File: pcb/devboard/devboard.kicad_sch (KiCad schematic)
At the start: 17 parts, among them J1 USB4110GFA, J3 Conn_01x16_Pin, J4 Conn_01x16_Pin, SW1 PTS526_SM15_SMTR2_LFS, SW2 PTS526_SM15_SMTR2_LFS, U1 ESP32-S3-MINI-1U, U2 IP4234CZ6, U3 ADP2108AUJ-3.3

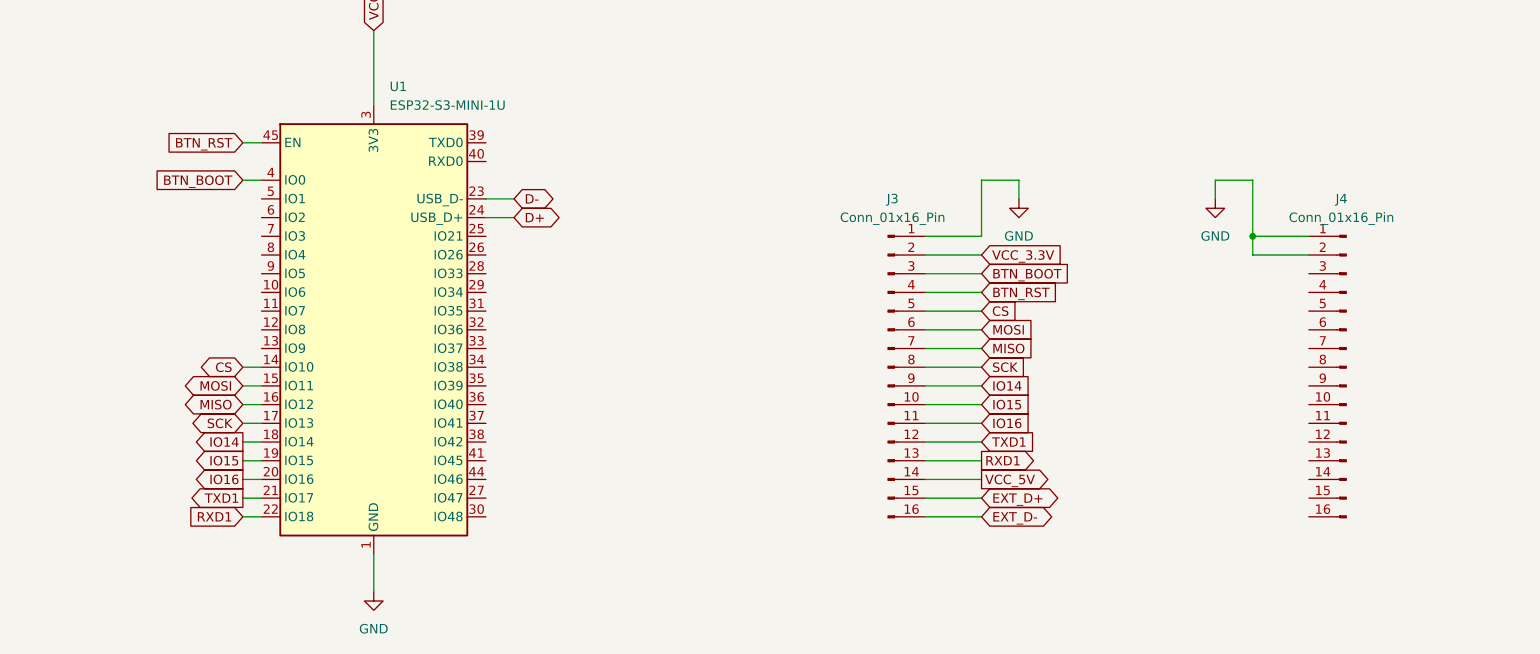
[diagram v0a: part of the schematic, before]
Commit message: connecting all remaining IOs
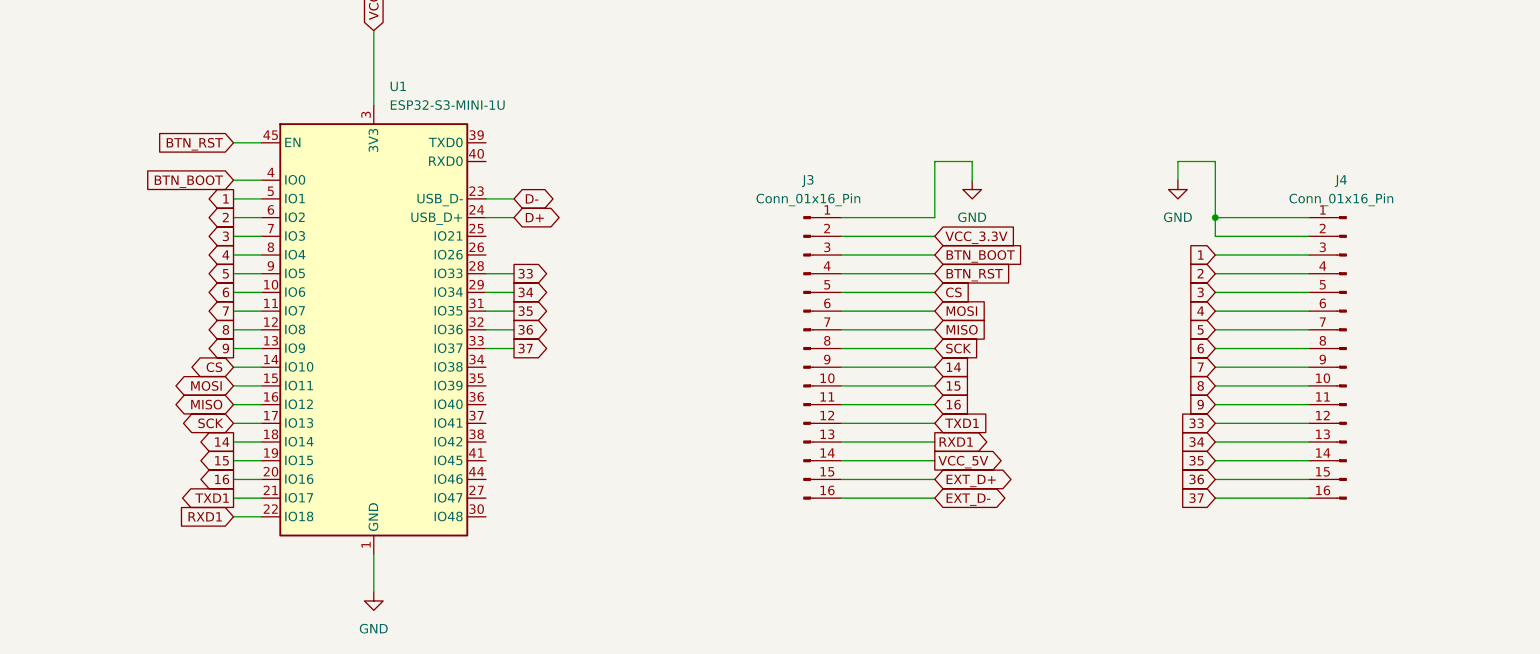
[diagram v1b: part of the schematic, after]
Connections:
- net 6: now reaches U1.10 (IO6)
- net 6: now also J4.8 (Pin_8)
- net 7: now reaches U1.11 (IO7)
- net 7: now also J4.9 (Pin_9)
- net 8: now reaches U1.12 (IO8)
- net 8: now also J4.10 (Pin_10)
- net 9: now reaches U1.13 (IO9)
- net 9: now also J4.11 (Pin_11)
- net 33: now reaches U1.28 (IO33)
- net 33: now also J4.12 (Pin_12)
- net 34: now reaches U1.29 (IO34)
- net 34: now also J4.13 (Pin_13)
- net 35: now reaches U1.31 (IO35)
- net 35: now also J4.14 (Pin_14)
- net 36: now reaches U1.32 (IO36)
- net 36: now also J4.15 (Pin_15)
- net 37: now reaches U1.33 (IO37)
- net 37: now also J4.16 (Pin_16)
- net 1: now reaches U1.5 (IO1)
- net 1: now also J4.3 (Pin_3)
- net 2: now reaches U1.6 (IO2)
- net 2: now also J4.4 (Pin_4)
- net 3: now reaches U1.7 (IO3)
- net 3: now also J4.5 (Pin_5)
- net 4: now reaches U1.8 (IO4)
- net 4: now also J4.6 (Pin_6)
- net 5: now reaches U1.9 (IO5)
- net 5: now also J4.7 (Pin_7)
- net IO14 renamed 14
- net IO15 renamed 15
- net IO16 renamed 16
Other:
- moved on the sheet: J3, J4

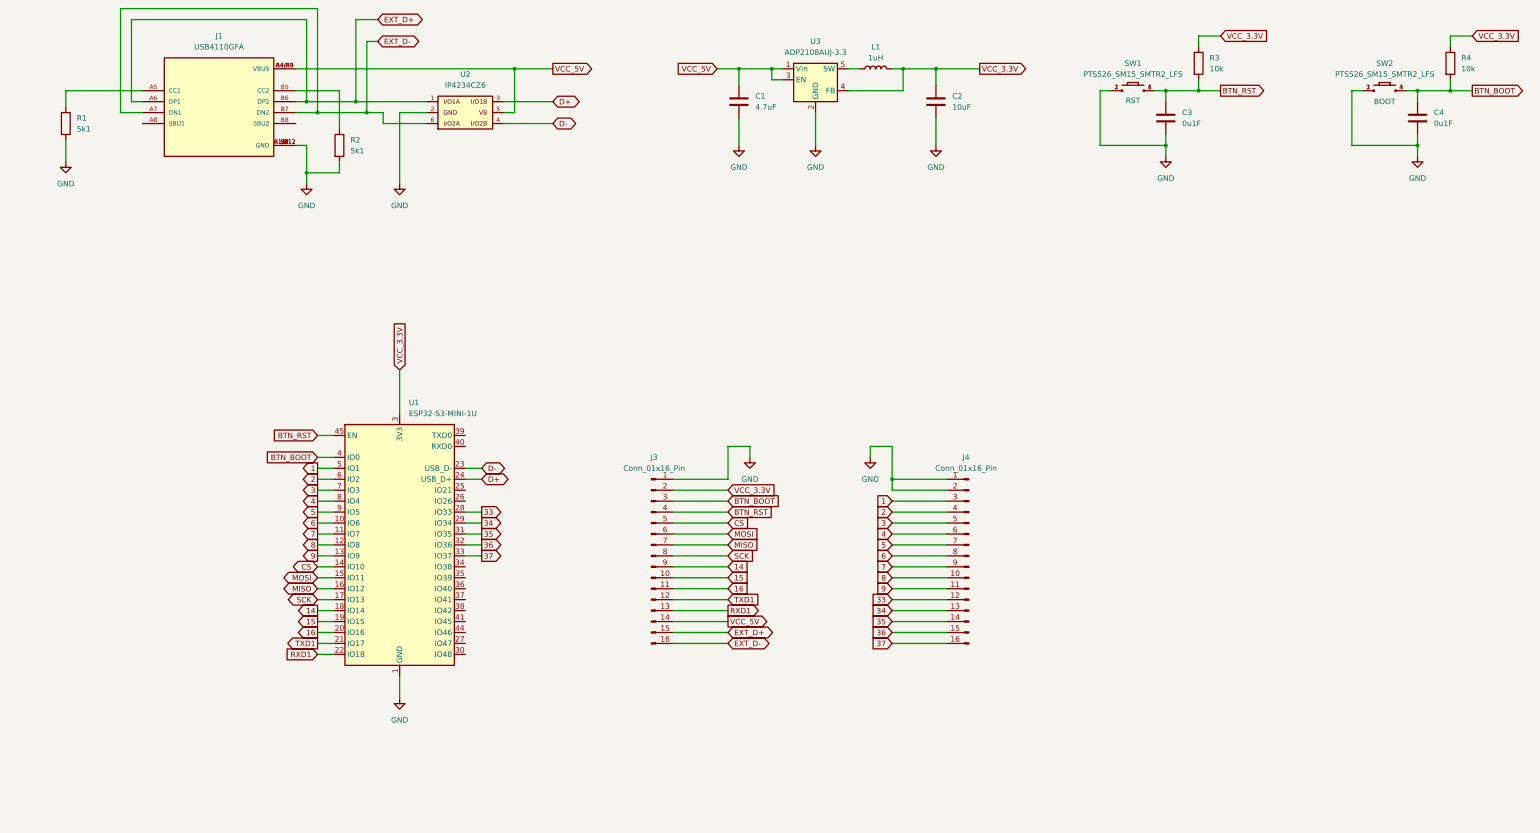
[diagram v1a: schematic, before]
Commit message: adding mouser part number to all parts
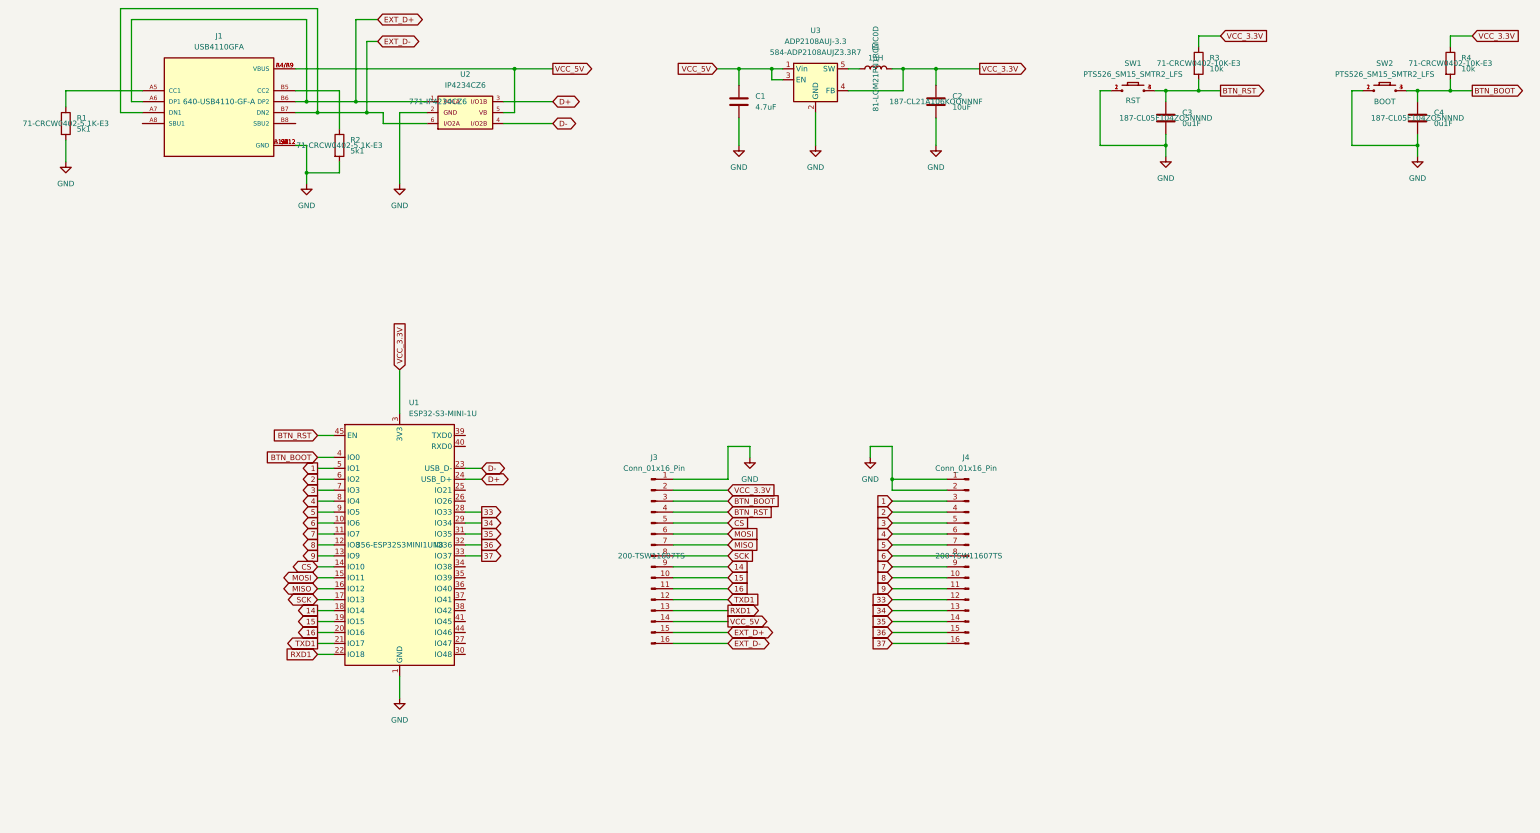
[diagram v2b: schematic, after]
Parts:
- C1: MOUSER_PART_NUMBER (none) -> 187-CL10A475KO8NNNC
- C2: MOUSER_PART_NUMBER (none) -> 187-CL21A106KOQNNNF
- C3, C4: MOUSER_PART_NUMBER (none) -> 187-CL05F104ZO5NNND
- J1: MOUSER_PART_NUMBER (none) -> 640-USB4110-GF-A
- J3, J4: MOUSER_PART_NUMBER (none) -> 200-TSW11607TS
- L1: MOUSER_PART_NUMBER (none) -> 81-LQM21PN1R0MC0D
- R1, R2: footprint (none) -> Resistor_SMD:R_0402_1005Metric; MOUSER_PART_NUMBER (none) -> 71-CRCW0402-5.1K-E3
- R3, R4: footprint (none) -> Resistor_SMD:R_0402_1005Metric; MOUSER_PART_NUMBER (none) -> 71-CRCW0402-10K-E3
- U1: MOUSER_PART_NUMBER (none) -> 356-ESP32S3MINI1UN8
- U2: MOUSER_PART_NUMBER (none) -> 771-IP4234CZ6
- U3: MOUSER_PART_NUMBER (none) -> 584-ADP2108AUJZ3.3R7
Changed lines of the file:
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@@
+			)
+		)
+		(property "MOUSER_PART_NUMBER" "771-IP4234CZ6"
+			(at 135.89 64.77 0)
+			(effects
+				(font
+					(size 1.27 1.27)
+				)
 			)
 		)
@@
 			)
 		)
-		(property "Footprint" ""
+		(property "Footprint" "Resistor_SMD:R_0402_1005Metric"
 			(at 47.752 69.85 90)
 			(effects
@@
 				)
 				(hide yes)
+			)
+		)
+		(property "MOUSER_PART_NUMBER" "71-CRCW0402-5.1K-E3"
+			(at 49.53 69.85 0)
+			(effects
+				(font
+					(size 1.27 1.27)
+				)
 			)
 		)
@@
 			)
 		)
-		(property "Footprint" ""
+		(property "Footprint" "Resistor_SMD:R_0402_1005Metric"
 			(at 369.062 55.88 90)
 			(effects
@@
 				)
 				(hide yes)
+			)
+		)
+		(property "MOUSER_PART_NUMBER" "71-CRCW0402-10K-E3"
+			(at 370.84 55.88 0)
+			(effects
+				(font
+					(size 1.27 1.27)
+				)
 			)
 		)
@@
 			)
 		)
+		(property "MOUSER_PART_NUMBER" "81-LQM21PN1R0MC0D"
+			(at 237.49 57.15 0)
+			(effects
+				(font
+					(size 1.27 1.27)
+				)
+			)
+		)
 		(pin "2"
 		)
@@
 			)
 		)
+		(property "MOUSER_PART_NUMBER" "640-USB4110-GF-A"
+			(at 85.09 64.77 0)
+			(effects
+				(font
+					(size 1.27 1.27)
+				)
+			)
+		)
 		(pin "S4"
 		)
@@
 			)
 		)
+		(property "MOUSER_PART_NUMBER" "356-ESP32S3MINI1UN8"
+			(at 127 167.64 0)
+			(effects
+				(font
+					(size 1.27 1.27)
+				)
+			)
+		)
 		(pin "62"
 		)
@@
 			)
 		)
+		(property "MOUSER_PART_NUMBER" "187-CL05F104ZO5NNND"
+			(at 363.22 68.58 0)
+			(effects
+				(font
+					(size 1.27 1.27)
+				)
+			)
+		)
 		(pin "1"
 		)
@@
 		(fields_autoplaced yes)
 		(property "Reference" "U3"
+			(at 223.52 48.26 0)
+			(effects
+				(font
+					(size 1.27 1.27)
+				)
+			)
+		)
+		(property "Value" "ADP2108AUJ-3.3"
 			(at 223.52 50.8 0)
-			(effects
-				(font
-					(size 1.27 1.27)
-				)
-			)
-		)
-		(property "Value" "ADP2108AUJ-3.3"
-			(at 223.52 53.34 0)
 			(effects
 				(font
@@
 				)
 				(hide yes)
+			)
+		)
+		(property "MOUSER_PART_NUMBER" "584-ADP2108AUJZ3.3R7"
+			(at 223.52 53.34 0)
+			(effects
+				(font
+					(size 1.27 1.27)
+				)
 			)
 		)
@@
 			)
 		)
-		(property "Footprint" ""
+		(property "Footprint" "Resistor_SMD:R_0402_1005Metric"
 			(at 111.252 74.93 90)
 			(effects
@@
 				)
 				(hide yes)
+			)
+		)
+		(property "MOUSER_PART_NUMBER" "71-CRCW0402-5.1K-E3"
+			(at 113.03 74.93 0)
+			(effects
+				(font
+					(size 1.27 1.27)
+				)
 			)
 		)
@@
 			)
 		)
+		(property "MOUSER_PART_NUMBER" "200-TSW11607TS"
+			(at 259.08 170.18 0)
+			(effects
+				(font
+					(size 1.27 1.27)
+				)
+			)
+		)
 		(pin "13"
 		)
@@
 			)
 		)
+		(property "MOUSER_PART_NUMBER" "187-CL21A106KOQNNNF"
+			(at 251.46 64.77 0)
+			(effects
+				(font
+					(size 1.27 1.27)
+				)
+			)
+		)
 		(pin "2"
 		)
@@
 			)
 		)
+		(property "MOUSER_PART_NUMBER" "200-TSW11607TS"
+			(at 185.42 170.18 0)
+			(effects
+				(font
+					(size 1.27 1.27)
+				)
+			)
+		)
 		(pin "13"
 		)
@@
 			)
 		)
+		(property "MOUSER_PART_NUMBER" "187-CL10A475KO8NNNC"
+			(at 205.74 64.77 0)
+			(effects
+				(font
+					(size 1.27 1.27)
+				)
+				(hide yes)
+			)
+		)
 		(pin "2"
 		)
@@
 			)
 		)
-		(property "Footprint" ""
+		(property "Footprint" "Resistor_SMD:R_0402_1005Metric"
 			(at 310.642 55.88 90)
 			(effects
@@
 				)
 				(hide yes)
+			)
+		)
+		(property "MOUSER_PART_NUMBER" "71-CRCW0402-10K-E3"
+			(at 312.42 55.88 0)
+			(effects
+				(font
+					(size 1.27 1.27)
+				)
 			)
 		)
@@
 			)
 		)
+		(property "MOUSER_PART_NUMBER" "187-CL05F104ZO5NNND"
+			(at 304.8 68.58 0)
+			(effects
+				(font
+					(size 1.27 1.27)
+				)
+			)
+		)

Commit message: designed pcb
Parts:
- added C5: 0u1F, Capacitor_SMD:C_0402_1005Metric, symbol Device:C
- C1: footprint (none) -> Capacitor_SMD:C_0603_1608Metric
- C2: footprint (none) -> Capacitor_SMD:C_0805_2012Metric
- C3, C4: footprint (none) -> Capacitor_SMD:C_0402_1005Metric
- L1: footprint (none) -> Inductor_SMD:L_0805_2012Metric
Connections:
- net 34: now also J4.15 (Pin_15); no longer J4.13 (Pin_13)
- net 36: now also J4.13 (Pin_13); no longer J4.15 (Pin_15)
- net 37: now also J4.12 (Pin_12); no longer J4.16 (Pin_16)
- net GND: now also J4.16 (Pin_16), C5.2
- net VCC_3.3V: now also C5.1
- net 33: no longer names the net of U1.28 (IO33)
- net 33: no longer J4.12 (Pin_12)
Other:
- title: (none) -> TRANCE Devboard

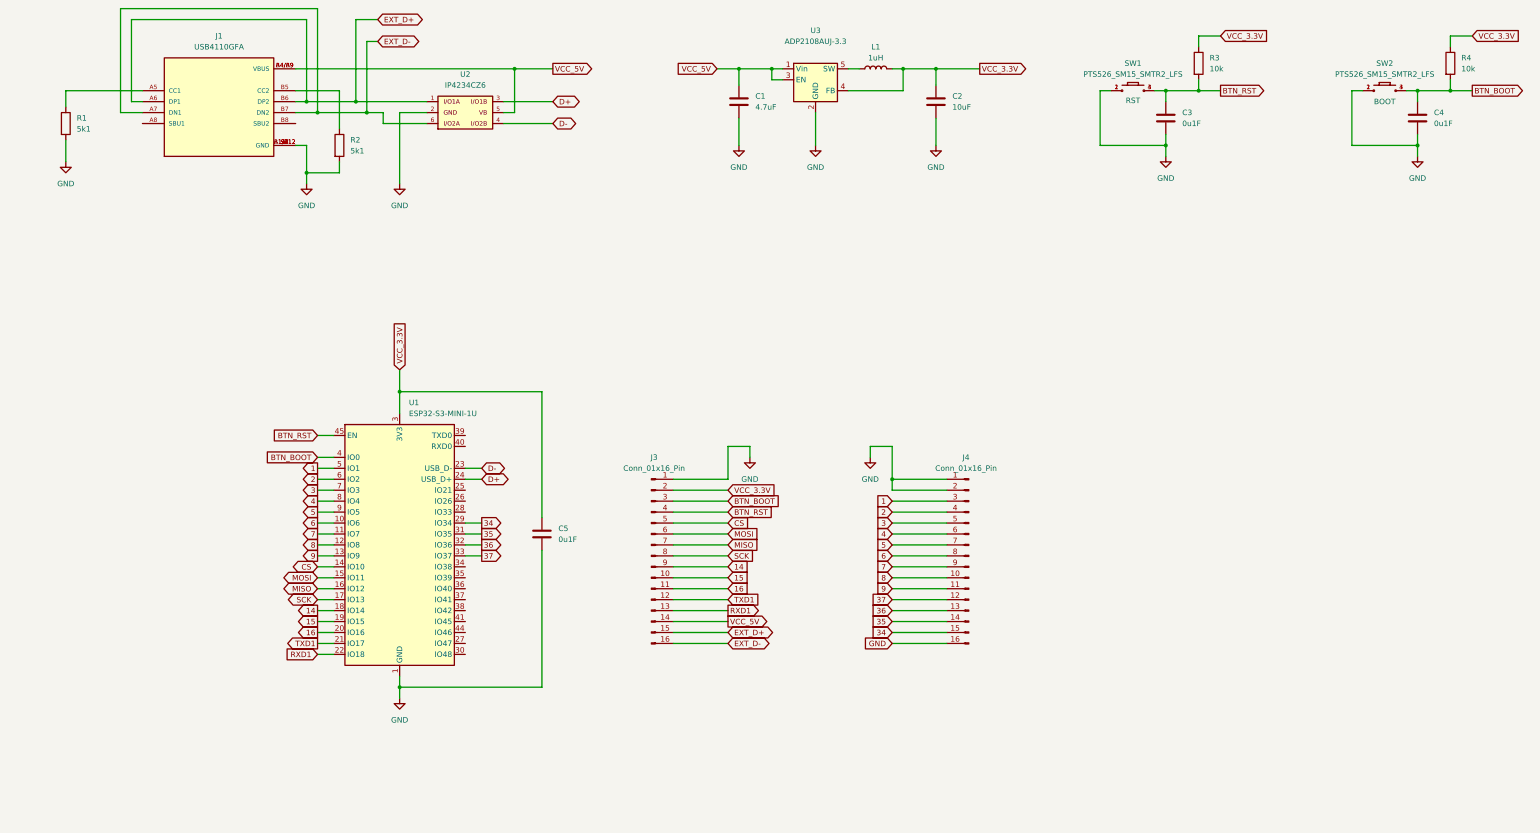
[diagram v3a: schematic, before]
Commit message: changing pinout to more gnd
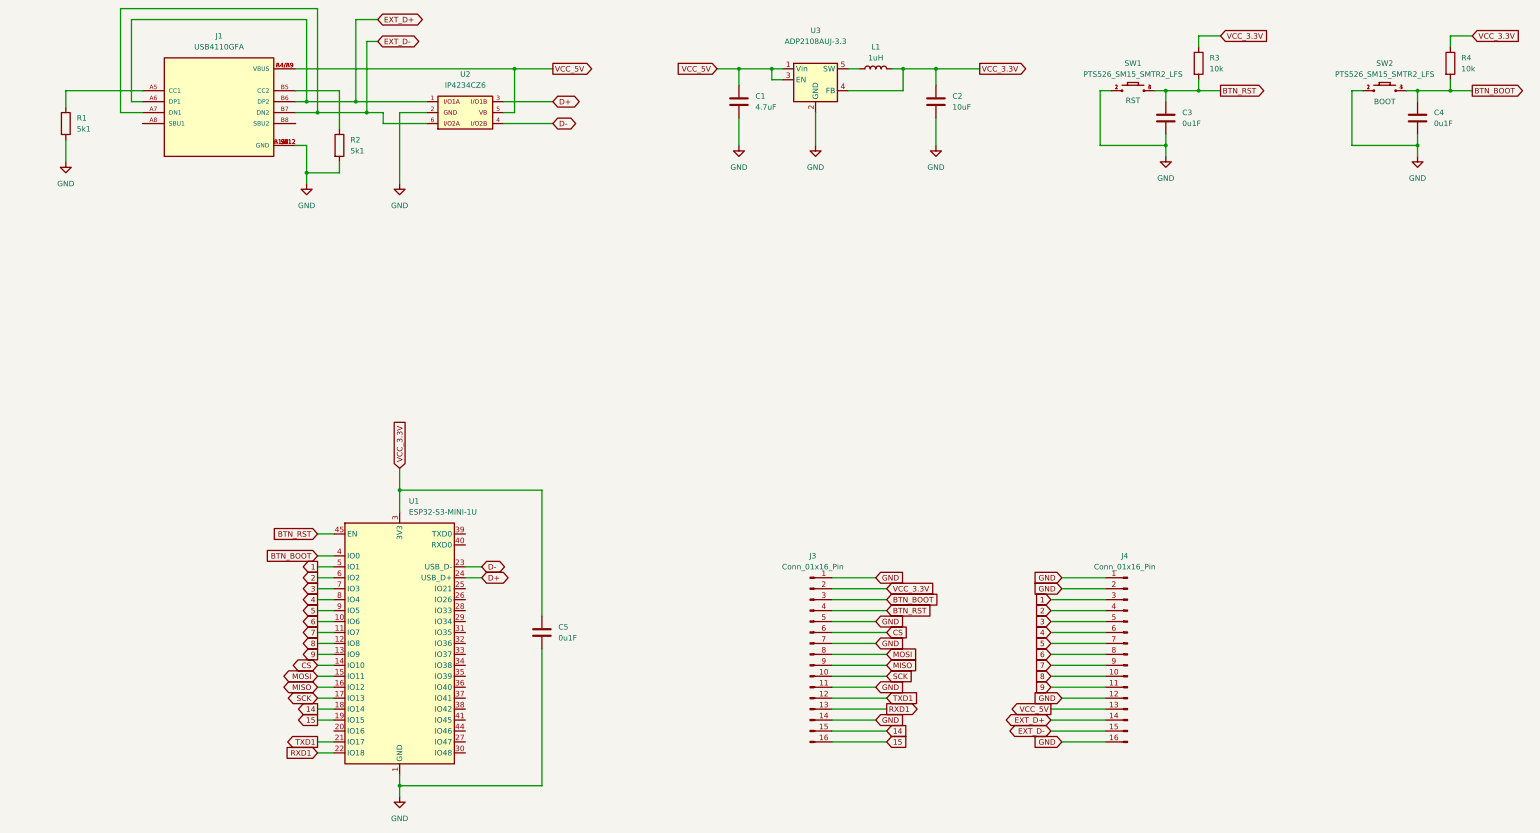
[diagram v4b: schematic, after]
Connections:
- net 14: now also J3.15 (Pin_15); no longer J3.9 (Pin_9)
- net 15: now also J3.16 (Pin_16); no longer J3.10 (Pin_10)
- net CS: now also J3.6 (Pin_6); no longer J3.5 (Pin_5)
- net EXT_D+: now also J4.14 (Pin_14); no longer J3.15 (Pin_15)
- net EXT_D-: now also J4.15 (Pin_15); no longer J3.16 (Pin_16)
- net GND: now also J3.11 (Pin_11), J3.14 (Pin_14), J3.5 (Pin_5), J3.7 (Pin_7), J4.12 (Pin_12)
- net MISO: now also J3.9 (Pin_9); no longer J3.7 (Pin_7)
- net MOSI: now also J3.8 (Pin_8); no longer J3.6 (Pin_6)
- net SCK: now also J3.10 (Pin_10); no longer J3.8 (Pin_8)
- net VCC_5V: now also J4.13 (Pin_13); no longer J3.14 (Pin_14)
- net 16: no longer names the net of U1.20 (IO16)
- net 16: no longer J3.11 (Pin_11)
- net 34: no longer names the net of U1.29 (IO34)
- net 34: no longer J4.15 (Pin_15)
- net 35: no longer names the net of U1.31 (IO35)
- net 35: no longer J4.14 (Pin_14)
- net 36: no longer names the net of U1.32 (IO36)
- net 36: no longer J4.13 (Pin_13)
- net 37: no longer names the net of U1.33 (IO37)
- net 37: no longer J4.12 (Pin_12)
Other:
- moved on the sheet: C5, J3, J4, U1
